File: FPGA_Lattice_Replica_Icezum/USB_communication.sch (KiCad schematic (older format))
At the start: 35 parts, among them J1 USB_Micro_Type_B, U3 FT2232H, U4 DSC1001, U5 93LC56C

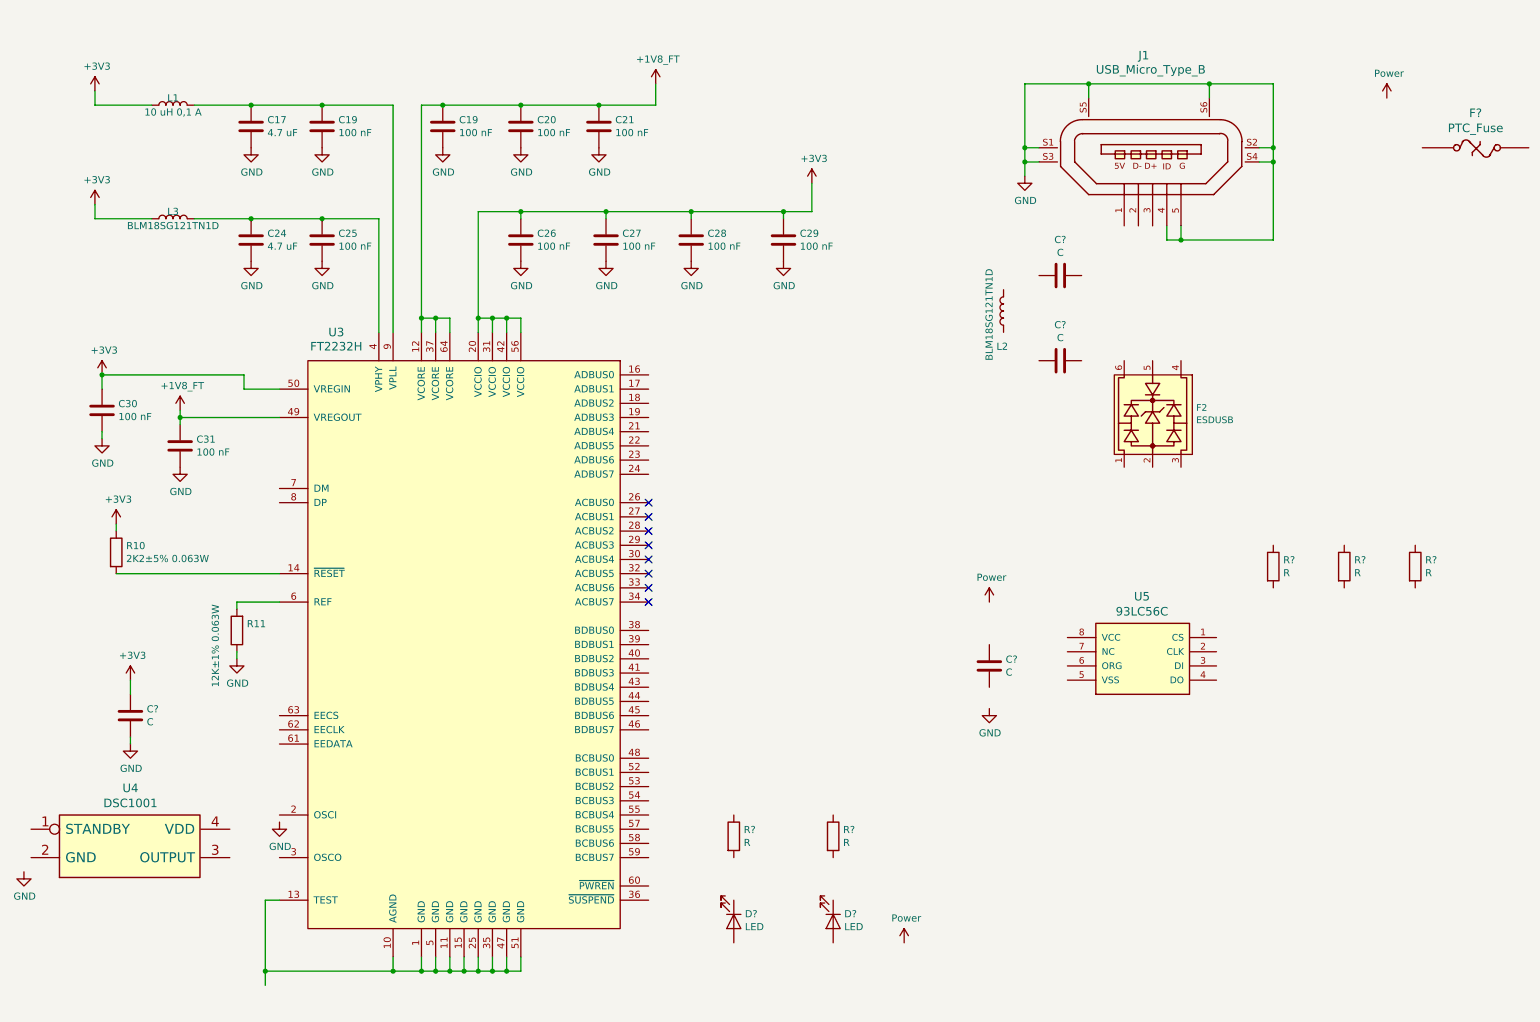
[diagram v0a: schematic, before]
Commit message: se completo esquema de perifericos y sockets. Se puso el mismo simbolo de referencia GND en el esquema de la fuente
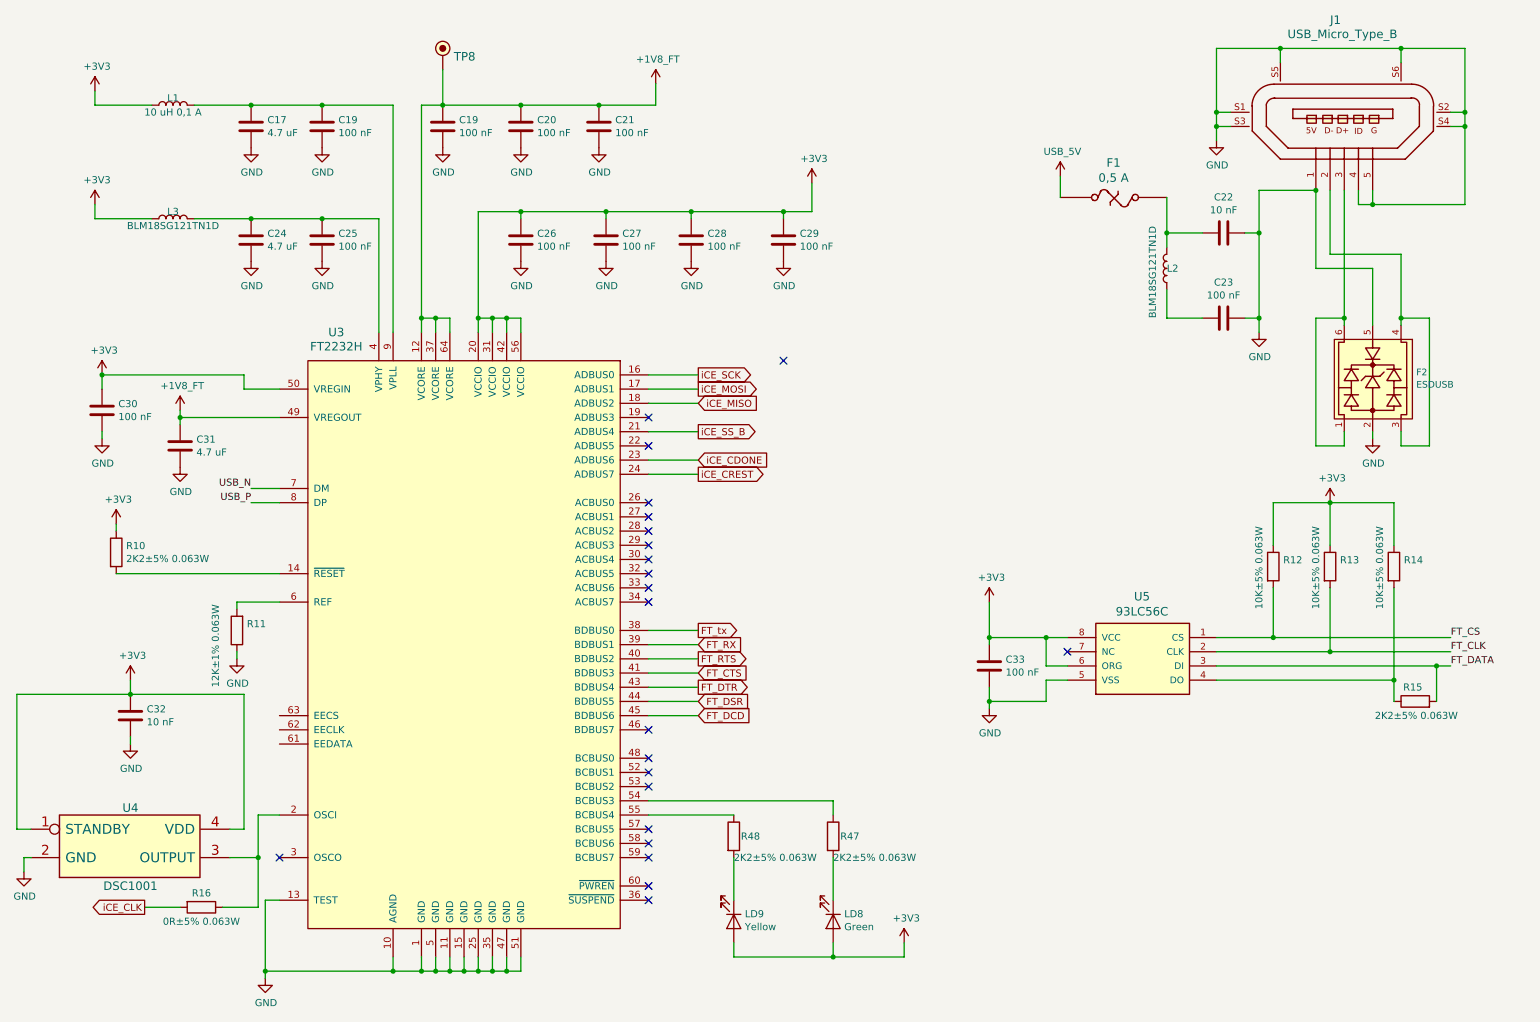
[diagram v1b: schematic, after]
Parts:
- added R15: 2K2±5% 0.063W, symbol Device:R
- added R16: 0R±5% 0.063W, symbol Device:R
- added TP8: TestPoint_Small, symbol icezum:TestPoint_Small
- C22, C32: renamed from C?; value C -> 10 nF
- C23, C33: renamed from C?; value C -> 100 nF
- C31: value 100 nF -> 4.7 uF
- F1: renamed from F?; value PTC_Fuse -> 0,5 A
- LD8: renamed from D?; value LED -> Green
- LD9: renamed from D?; value LED -> Yellow
- R12, R13, R14: renamed from R?; value R -> 10K±5% 0.063W
- R47, R48: renamed from R?; value R -> 2K2±5% 0.063W
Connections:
- net +1V8_FT: now also TP8.1 (tp)
- net +3V3: now also C33.1, LD8.2 (A), LD9.2 (A), R12.1, R13.1, R14.1, U4.1 (STANDBY), U4.4 (VDD), U5.6 (ORG), U5.8 (VCC)
- net GND: now also C22.1, C23.1, C33.2, F2.2, F2.5, J1.1 (P1), U3.1 (GND), U3.10 (AGND), U3.11 (GND), U3.13 (TEST), U3.15 (GND), U3.25 (GND), U3.35 (GND), U3.47 (GND), U3.5 (GND), U3.51 (GND), U4.2 (GND), U5.5 (VSS)
- net iCE_SCK: now reaches U3.16 (ADBUS0)
- net iCE_MOSI: now reaches U3.17 (ADBUS1)
- net iCE_MISO: now reaches U3.18 (ADBUS2)
- net at U3.2 (OSCI): now also U4.3 (OUTPUT), R16.1
- net iCE_SS_B: now reaches U3.21 (ADBUS4)
- net iCE_CDONE: now reaches U3.23 (ADBUS6)
- net iCE_CREST: now reaches U3.24 (ADBUS7)
- net FT_tx: now reaches U3.38 (BDBUS0)
- net FT_RX: now reaches U3.39 (BDBUS1)
- net FT_RTS: now reaches U3.40 (BDBUS2)
- net FT_CTS: now reaches U3.41 (BDBUS3)
- net FT_DTR: now reaches U3.43 (BDBUS4)
- net FT_DSR: now reaches U3.44 (BDBUS5)
- net FT_DCD: now reaches U3.45 (BDBUS6)
- net at U3.54 (BCBUS3): now also R47.1
- net at U3.55 (BCBUS4): now also R48.1
- net USB_N: now reaches U3.7 (DM)
- net USB_P: now reaches U3.8 (DP)
- net FT_CS: now reaches U5.1 (CS)
- net FT_CS: now also R12.2
- net FT_CLK: now reaches U5.2 (CLK)
- net FT_CLK: now also R13.2
- net FT_DATA: now reaches U5.3 (DI)
- net FT_DATA: now also R15.2
- net at U5.4 (DO): now also R14.2, R15.1
- net at J1.2 (P2): now also F2.3, F2.4
- net at J1.3 (P3): now also F2.1, F2.6
- net at L2.1: now also C23.2
- net at L2.2: now also C22.2, F1.2
- net USB_5V: now reaches F1.1
- net at R48.2: now also LD9.1 (K)
- net at R47.2: now also LD8.1 (K)
- new net iCE_CLK: R16.2
- no-connect marks 8 -> 22
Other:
- moved on the sheet: C22, C23, F1, F2, J1, L2, R13, R14

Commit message: se ejecuto y se corrigio electrical rules check
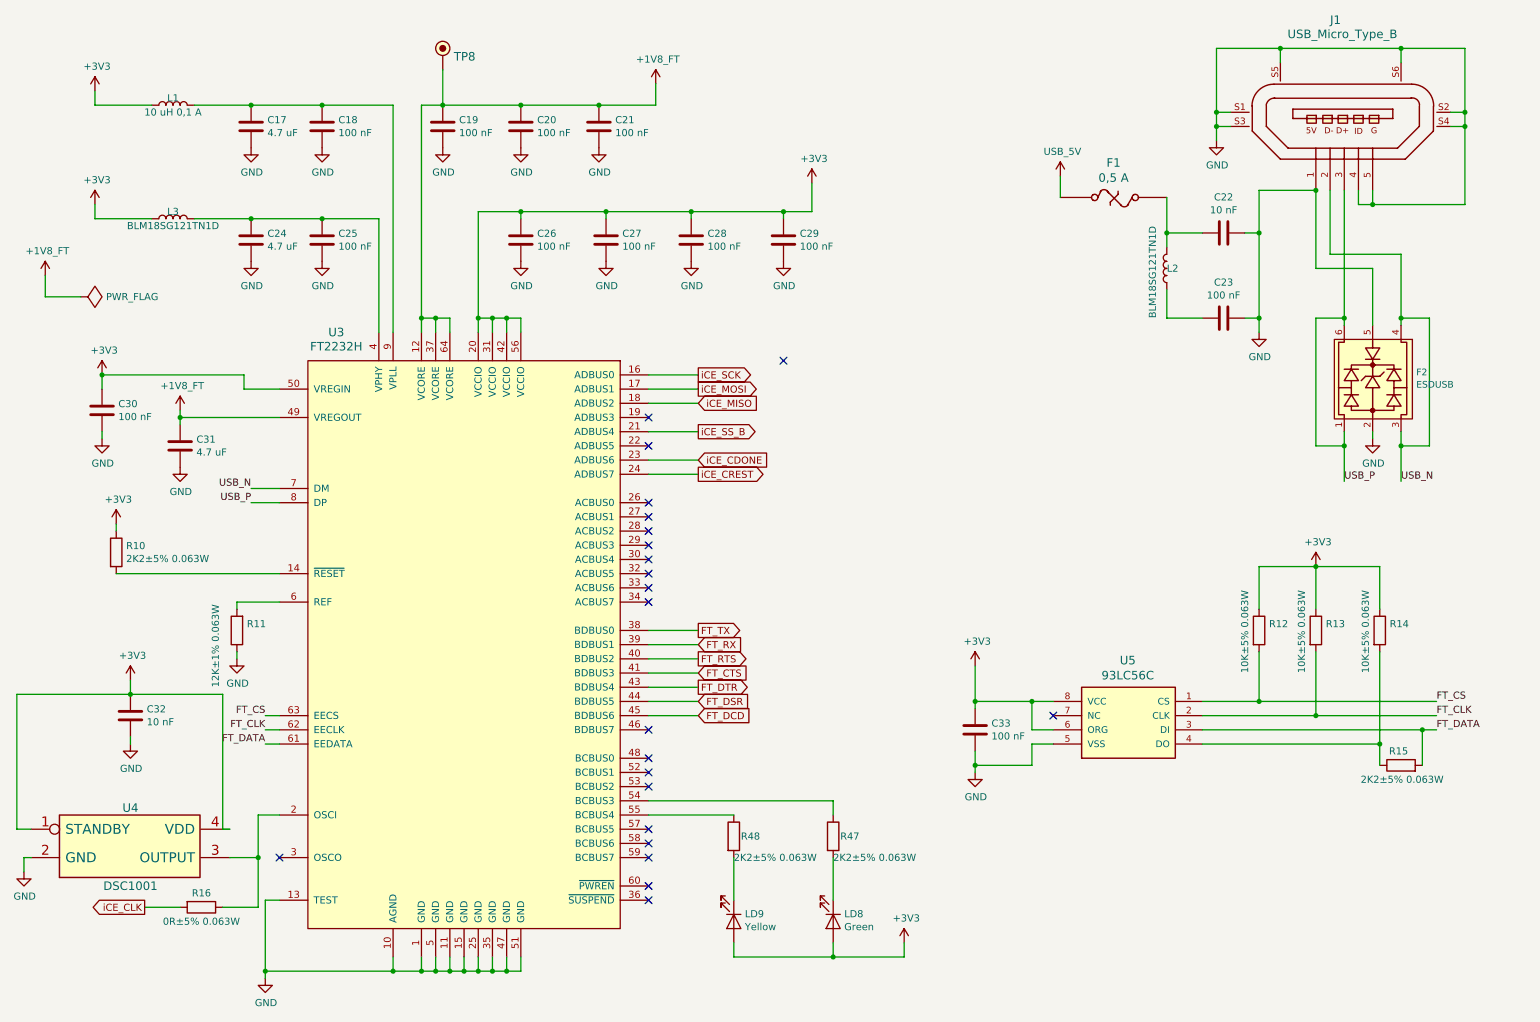
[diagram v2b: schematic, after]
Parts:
- renumbered C19 to C18
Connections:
- net FT_CLK: now also U3.62 (EECLK)
- net FT_CS: now also U3.63 (EECS)
- net FT_DATA: now also U3.61 (EEDATA)
- net USB_N: now also F2.3, F2.4, J1.2 (P2)
- net USB_P: now also F2.1, F2.6, J1.3 (P3)
- net FT_tx renamed FT_TX
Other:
- moved on the sheet: C33, R12, R13, R14, R15, U5

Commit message: se comenzo asignacion de footprints
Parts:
- C17, C22, C24, C31: footprint (none) -> footprints:C_0603
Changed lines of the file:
@@
 F 0 "U5" H 8375 5689 60  0000 C CNN
 F 1 "93LC56C" H 8375 5583 60  0000 C CNN
-F 2 "" H 8050 5500 60  0000 C CNN
+F 2 "" H 8050 5500 60  0001 C CNN
 F 3 "" H 8050 5500 60  0000 C CNN
 	1    8050 5500
@@
 F 0 "J1" H 9100 800 60  0000 R CNN
 F 1 "USB_Micro_Type_B" H 9400 900 60  0000 R CNN
-F 2 "" H 9450 2000 60  0000 C CNN
+F 2 "" H 9450 2000 60  0001 C CNN
 F 3 "" H 9450 2000 60  0000 C CNN
 	1    9450 2000
@@
 F 0 "F2" V 10631 3057 47  0000 L CNN
 F 1 "ESDUSB" V 10718 3057 47  0000 L CNN
-F 2 "" H 10350 3050 47  0000 C CNN
+F 2 "" H 10350 3050 47  0001 C CNN
 F 3 "" H 10350 3050 47  0000 C CNN
 	1    10300 2950
@@
 F 0 "F1" H 8275 2294 60  0000 C CNN
 F 1 "0,5 A" H 8275 2188 60  0000 C CNN
-F 2 "" H 7900 2050 60  0000 C CNN
+F 2 "" H 7900 2050 60  0001 C CNN
 F 3 "" H 7900 2050 60  0000 C CNN
 	1    7900 2050
@@
 F 0 "C22" V 8798 2300 50  0000 C CNN
 F 1 "10 nF" V 8889 2300 50  0000 C CNN
-F 2 "" H 9088 2150 50  0001 C CNN
+F 2 "footprints:C_0603" H 9088 2150 50  0001 C CNN
 F 3 "~" H 9050 2300 50  0001 C CNN
 	1    9050 2300
@@
 F 0 "C24" H 2315 2396 50  0000 L CNN
 F 1 "4.7 uF" H 2315 2305 50  0000 L CNN
-F 2 "" H 2238 2200 50  0001 C CNN
+F 2 "footprints:C_0603" H 2238 2200 50  0001 C CNN
 F 3 "~" H 2200 2350 50  0001 C CNN
 	1    2200 2350
@@
 F 0 "C17" H 2315 1596 50  0000 L CNN
 F 1 "4.7 uF" H 2315 1505 50  0000 L CNN
-F 2 "" H 2238 1400 50  0001 C CNN
+F 2 "footprints:C_0603" H 2238 1400 50  0001 C CNN
 F 3 "~" H 2200 1550 50  0001 C CNN
 	1    2200 1550
@@
 F 0 "C31" H 1815 3846 50  0000 L CNN
 F 1 "4.7 uF" H 1815 3755 50  0000 L CNN
-F 2 "" H 1738 3650 50  0001 C CNN
+F 2 "footprints:C_0603" H 1738 3650 50  0001 C CNN
 F 3 "~" H 1700 3800 50  0001 C CNN
 	1    1700 3800
@@
 F 0 "U4" H 1350 6450 60  0000 C CNN
 F 1 "DSC1001" H 1350 5900 60  0000 C CNN
-F 2 "" H 850 6400 60  0000 C CNN
+F 2 "" H 850 6400 60  0001 C CNN
 F 3 "" H 850 6400 60  0000 C CNN
 	1    850  6400
@@
 F 0 "U3" H 2800 7400 60  0000 C CNN
 F 1 "FT2232H" H 2800 7300 60  0000 C CNN
-F 2 "" H 3600 5300 60  0000 C CNN
+F 2 "" H 3600 5300 60  0001 C CNN
 F 3 "" H 3600 5300 60  0000 C CNN
 	1    3700 5200
@@
 F 0 "TP8" H 3628 1242 60  0000 L CNN
 F 1 "TestPoint_Small" H 3550 1050 60  0001 C CNN
-F 2 "" H 3550 1150 60  0000 C CNN
+F 2 "" H 3550 1150 60  0001 C CNN
 F 3 "" H 3550 1150 60  0000 C CNN
 	1    3550 1150
